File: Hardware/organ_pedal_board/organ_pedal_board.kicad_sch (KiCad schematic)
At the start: 40 parts, among them J1 Conn_01x04, J2 NMJ6HFD2, J3 NMJ6HFD2, J4 ADS1115_conn, SW1 SW_Push, SW2 SW_Push, SW3 SW_Push, SW4 SW_Push, SW5 SW_Push, SW6 SW_Push, SW7 SW_Push, SW8 SW_Push, SW9 SW_Push, U1 MCP6002-xSN

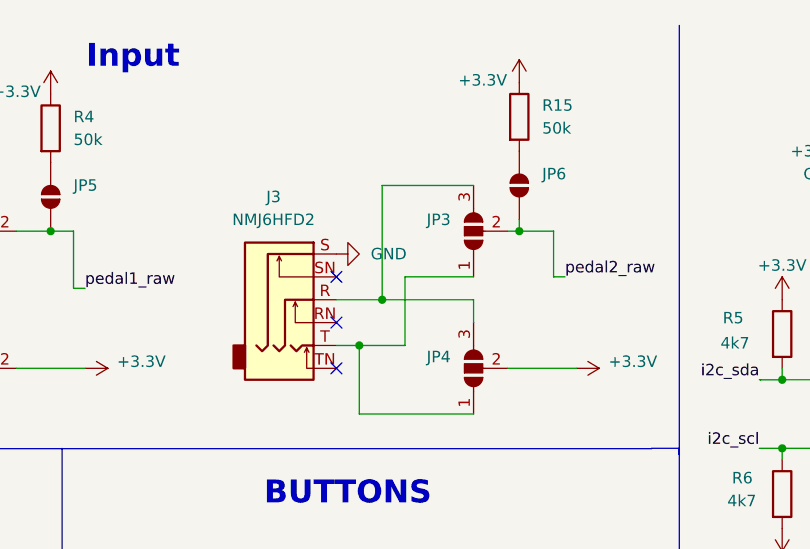
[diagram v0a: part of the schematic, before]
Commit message: Fix active layer and update junctions in organ pedal board schematic
- Changed active layer from 5 to 0 in the KiCad project file.
- Removed an unnecessary junction and added a new junction at updated coordinates.
- Adjusted wire connections to reflect new junction positions.
- Updated footprint properties for several components to ensure correct part references.
- Cleaned up redundant wire definitions to improve schematic clarity.
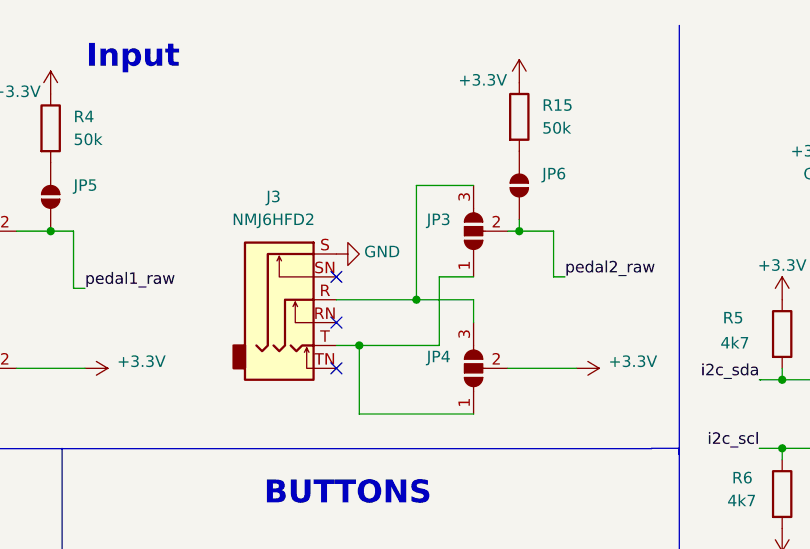
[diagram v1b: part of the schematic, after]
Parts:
- JP1, JP2, JP3, JP4: footprint (none) -> Jumper:SolderJumper-3_P1.3mm_Open_RoundedPad1.0x1.5mm
- JP5, JP6: footprint (none) -> Jumper:SolderJumper-2_P1.3mm_Open_RoundedPad1.0x1.5mm
- R15, R4: footprint (none) -> Resistor_THT:R_Axial_DIN0207_L6.3mm_D2.5mm_P2.54mm_Vertical
- R17: footprint Resistor_THT:R_Axial_DIN0207_L6.3mm_D2.5mm_P5.08mm_Vertical -> Resistor_THT:R_Axial_DIN0207_L6.3mm_D2.5mm_P2.54mm_Vertical
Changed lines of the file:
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@@
 	)
 	(junction
-		(at 180.34 43.18)
-		(diameter 0)
-		(color 0 0 0 0)
-	)
-	(junction
 		(at 224.79 52.07)
 		(diameter 0)
@@
 	)
 	(junction
+		(at 184.15 43.18)
+		(diameter 0)
+		(color 0 0 0 0)
+	)
+	(junction
 		(at 168.91 93.98)
 		(diameter 0)
@@
 	(wire
 		(pts
-			(xy 180.34 30.48) (xy 180.34 43.18)
+			(xy 184.15 30.48) (xy 184.15 43.18)
 		)
 		(stroke
@@
 	(wire
 		(pts
-			(xy 190.5 40.64) (xy 182.88 40.64)
+			(xy 190.5 40.64) (xy 186.69 40.64)
 		)
 		(stroke
@@
 	(wire
 		(pts
-			(xy 182.88 48.26) (xy 177.8 48.26)
+			(xy 186.69 48.26) (xy 177.8 48.26)
 		)
 		(stroke
@@
 	(wire
 		(pts
-			(xy 182.88 40.64) (xy 182.88 48.26)
+			(xy 186.69 40.64) (xy 186.69 48.26)
 		)
 		(stroke
@@
 		)
 	)
+	(wire
+		(pts
+			(xy 184.15 43.18) (xy 190.5 43.18)
+		)
+		(stroke
+			(width 0)
+			(type default)
+		)
+	)
 	(polyline
 		(pts
@@
 	(wire
 		(pts
-			(xy 180.34 43.18) (xy 190.5 43.18)
-		)
-		(stroke
-			(width 0)
-			(type default)
-		)
-	)
-	(wire
-		(pts
 			(xy 224.79 50.8) (xy 224.79 52.07)
 		)
@@
 	(wire
 		(pts
-			(xy 180.34 30.48) (xy 190.5 30.48)
+			(xy 184.15 30.48) (xy 190.5 30.48)
 		)
 		(stroke
@@
 	(wire
 		(pts
-			(xy 175.26 43.18) (xy 180.34 43.18)
+			(xy 175.26 43.18) (xy 184.15 43.18)
 		)
 		(stroke
@@
 			)
 		)
-		(property "Footprint" ""
+		(property "Footprint" "Jumper:SolderJumper-3_P1.3mm_Open_RoundedPad1.0x1.5mm"
 			(at 190.5 35.56 0)
 			(effects
@@
 			)
 		)
-		(property "Footprint" ""
+		(property "Footprint" "Jumper:SolderJumper-3_P1.3mm_Open_RoundedPad1.0x1.5mm"
 			(at 135.89 50.8 0)
 			(effects
@@
 			)
 		)
-		(property "Footprint" ""
+		(property "Footprint" "Jumper:SolderJumper-2_P1.3mm_Open_RoundedPad1.0x1.5mm"
 			(at 195.58 30.48 0)
 			(effects
@@
 			)
 		)
-		(property "Footprint" ""
+		(property "Footprint" "Jumper:SolderJumper-2_P1.3mm_Open_RoundedPad1.0x1.5mm"
 			(at 143.51 31.75 0)
 			(effects
@@
 			)
 		)
-		(property "Footprint" ""
+		(property "Footprint" "Resistor_THT:R_Axial_DIN0207_L6.3mm_D2.5mm_P2.54mm_Vertical"
 			(at 193.802 22.86 90)
 			(effects
@@
 			)
 		)
-		(property "Footprint" "Resistor_THT:R_Axial_DIN0207_L6.3mm_D2.5mm_P5.08mm_Vertical"
+		(property "Footprint" "Resistor_THT:R_Axial_DIN0207_L6.3mm_D2.5mm_P2.54mm_Vertical"
 			(at 55.372 38.1 90)
 			(effects
@@
 			)
 		)
-		(property "Footprint" ""
+		(property "Footprint" "Jumper:SolderJumper-3_P1.3mm_Open_RoundedPad1.0x1.5mm"
 			(at 135.89 35.56 0)
 			(effects
@@
 		(on_board yes)
 		(dnp no)
-		(fields_autoplaced yes)
 		(property "Reference" "#PWR014"
 			(at 181.61 38.1 0)
@@
 		)
 		(property "Value" "GND"
-			(at 179.07 38.0999 90)
+			(at 180.34 38.608 90)
 			(effects
 				(font
 					(size 1.27 1.27)
 				)
-				(justify right)
+				(justify top)
 			)
 		)
@@
 			)
 		)
-		(property "Footprint" ""
+		(property "Footprint" "Jumper:SolderJumper-3_P1.3mm_Open_RoundedPad1.0x1.5mm"
 			(at 190.5 50.8 0)
 			(effects
@@
 			)
 		)
-		(property "Footprint" ""
+		(property "Footprint" "Resistor_THT:R_Axial_DIN0207_L6.3mm_D2.5mm_P2.54mm_Vertical"
 			(at 141.732 24.13 90)
 			(effects
